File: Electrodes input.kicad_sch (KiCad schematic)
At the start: 36 parts, among them J2 Conn_01x26_Pin, U10 TPD4E1B06DCKR, U2 TPD4E1B06DCKR, U3 TPD4E1B06DCKR, U4 TPD4E1B06DCKR, U5 TPD4E1B06DCKR, U9 TPD4E1B06DCKR

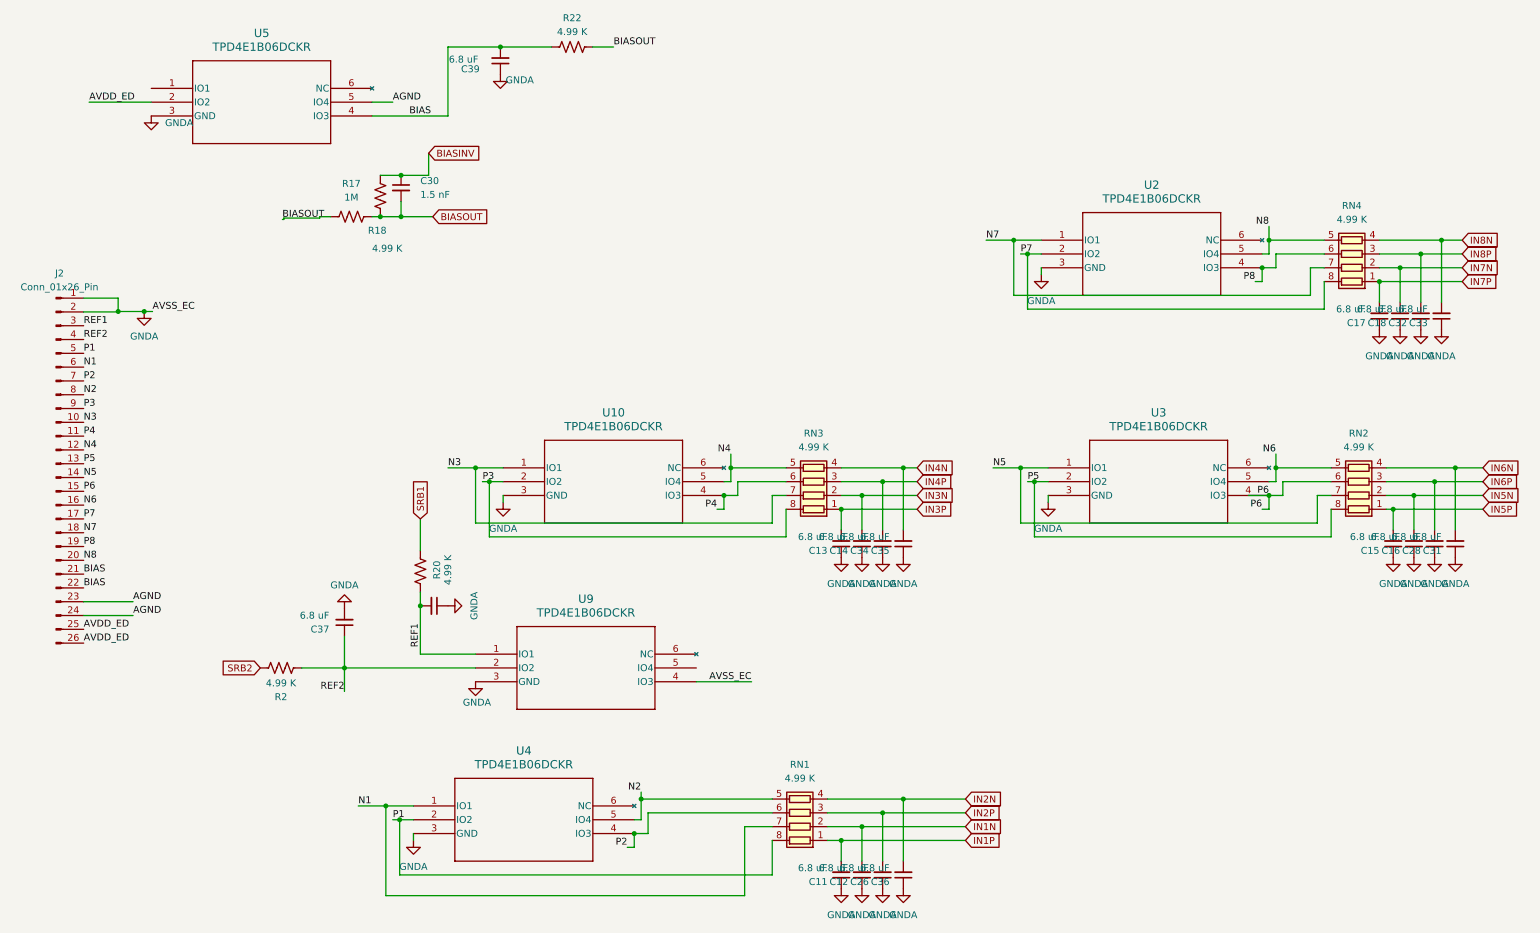
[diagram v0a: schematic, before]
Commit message: redone analog inputs, adjusted all footprints to match real components, added library for potential implementation of 4 element capacitor arrays
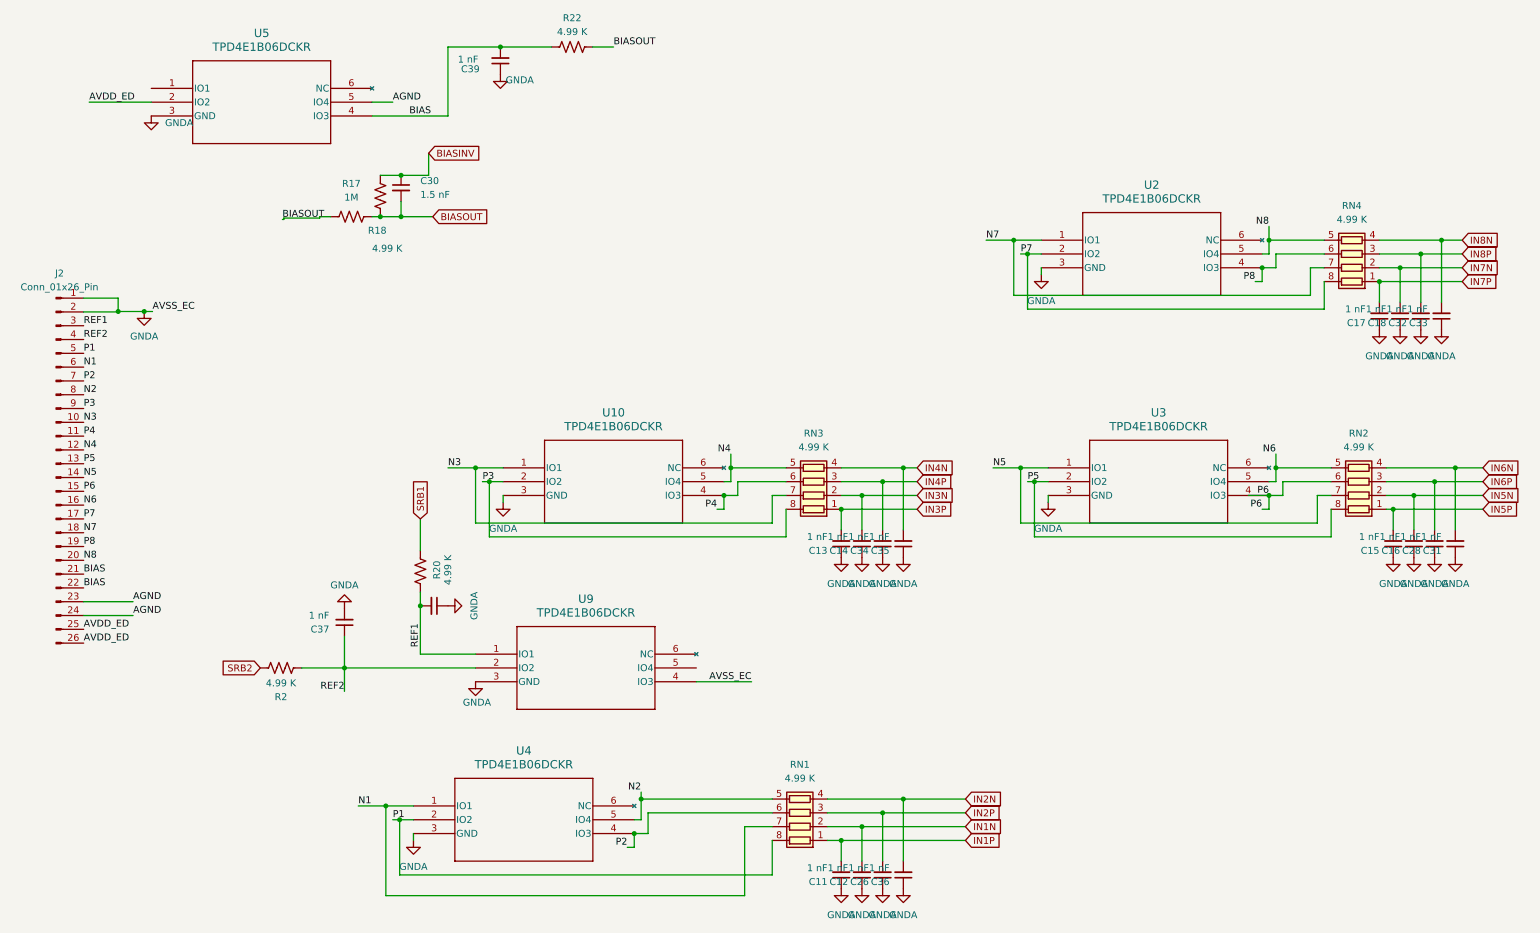
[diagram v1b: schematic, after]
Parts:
- C11, C12, C13, C14, C15, C16, C17, C18, C26, C28, C31, C32, C33, C34, C35, C36, C37, C38, C39: value 6.8 uF -> 1 nF
- RN4: footprint Resistor_SMD:R_Array_Convex_4x0402 -> Resistor_SMD:R_Array_Convex_4x0603
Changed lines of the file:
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@@
 			)
 		)
-		(property "Value" "6.8 uF"
+		(property "Value" "1 nF"
 			(at 67.056 123.6917 0)
 			(effects
@@
 			)
 		)
-		(property "Value" "6.8 uF"
+		(property "Value" "1 nF"
 			(at 158.75 109.2137 0)
 			(effects
@@
 			)
 		)
-		(property "Value" "6.8 uF"
+		(property "Value" "1 nF"
 			(at 261.62 67.3037 0)
 			(effects
@@
 			)
 		)
-		(property "Value" "6.8 uF"
+		(property "Value" "1 nF"
 			(at 162.56 170.1737 0)
 			(effects
@@
 			)
 		)
-		(property "Value" "6.8 uF"
+		(property "Value" "1 nF"
 			(at 267.97 109.2137 0)
 			(effects
@@
 			)
 		)
-		(property "Footprint" "Resistor_SMD:R_Array_Convex_4x0402"
+		(property "Footprint" "Resistor_SMD:R_Array_Convex_4x0603"
 			(at 255.27 50.165 90)
 			(effects
@@
 			)
 		)
-		(property "Value" "6.8 uF"
+		(property "Value" "1 nF"
 			(at 170.18 170.1737 0)
 			(effects
@@
 			)
 		)
-		(property "Value" "6.8 uF"
+		(property "Value" "1 nF"
 			(at 269.24 67.3037 0)
 			(effects
@@
 			)
 		)
-		(property "Value" "6.8 uF"
+		(property "Value" "1 nF"
 			(at 166.37 109.2137 0)
 			(effects
@@
 			)
 		)
-		(property "Value" "6.8 uF"
+		(property "Value" "1 nF"
 			(at 162.56 109.2137 0)
 			(effects
@@
 			)
 		)
-		(property "Value" "6.8 uF"
+		(property "Value" "1 nF"
 			(at 166.37 170.1737 0)
 			(effects
@@
 			)
 		)
-		(property "Value" "6.8 uF"
+		(property "Value" "1 nF"
 			(at 170.18 109.2137 0)
 			(effects
@@
 			)
 		)
-		(property "Value" "6.8 uF"
+		(property "Value" "1 nF"
 			(at 271.78 109.2137 0)
 			(effects
@@
 			)
 		)
-		(property "Value" "6.8 uF"
+		(property "Value" "1 nF"
 			(at 158.75 170.1737 0)
 			(effects
@@
 			)
 		)
-		(property "Value" "6.8 uF"
+		(property "Value" "1 nF"
 			(at 264.16 109.2137 0)
 			(effects
@@
 			)
 		)
-		(property "Value" "6.8 uF"
+		(property "Value" "1 nF"
 			(at 257.81 67.3037 0)
 			(effects
@@
 			)
 		)
-		(property "Value" "6.8 uF"
+		(property "Value" "1 nF"
 			(at 260.35 109.2137 0)
 			(effects
@@
 			)
 		)
-		(property "Value" "6.8 uF"
+		(property "Value" "1 nF"
 			(at 86.106 125.984 0)
 			(effects
@@
 			)
 		)
-		(property "Value" "6.8 uF"
+		(property "Value" "1 nF"
 			(at 94.488 21.336 0)
 			(effects
@@
 			)
 		)
-		(property "Value" "6.8 uF"
+		(property "Value" "1 nF"
 			(at 265.43 67.3037 0)
 			(effects
